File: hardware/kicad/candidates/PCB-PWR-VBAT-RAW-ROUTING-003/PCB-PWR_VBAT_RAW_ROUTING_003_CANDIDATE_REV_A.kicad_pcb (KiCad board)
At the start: 4 copper layers, 90 x 60 mm, 66 parts, among them J1 43045-0213, J2 43045-1202, Q1 CSD18540Q5B, U1 LM74700QDBVRQ1, U2 INA226AIDGSR, U3 LMR604403SRAKR, U4 LMR604403SRAKR, U5 TPS7A2018PDBVR

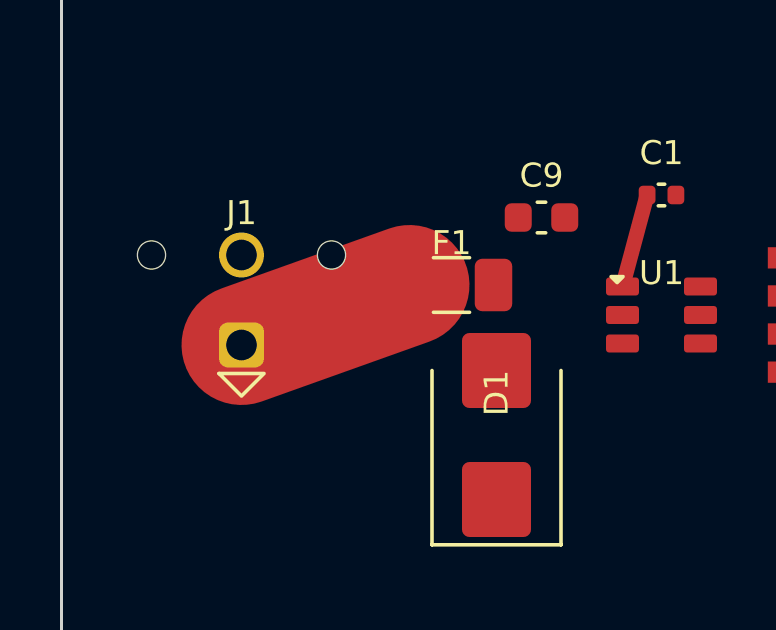
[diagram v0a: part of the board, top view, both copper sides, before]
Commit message: hardware: clear F1.2 around VBAT_RAW candidate
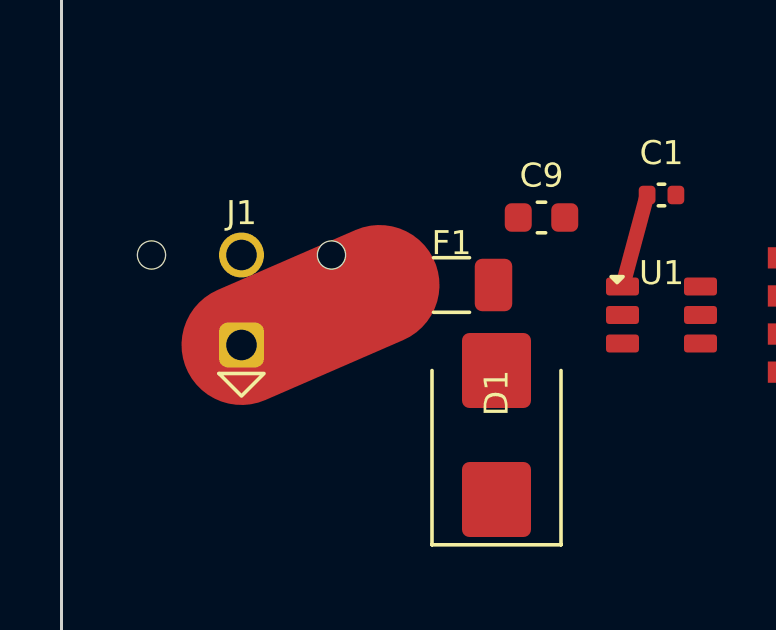
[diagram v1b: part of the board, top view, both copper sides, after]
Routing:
- net VBAT_RAW: track 5.95 -> 5.02 mm
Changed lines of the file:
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@@
 	(segment
 		(start 6 31)
-		(end 11.6 29)
+		(end 10.6 29)
 		(width 4)
 		(layer "F.Cu")
